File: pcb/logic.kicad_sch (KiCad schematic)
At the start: 8 parts, among them U3 74HC02, U4 74HC08, U5 74HC02

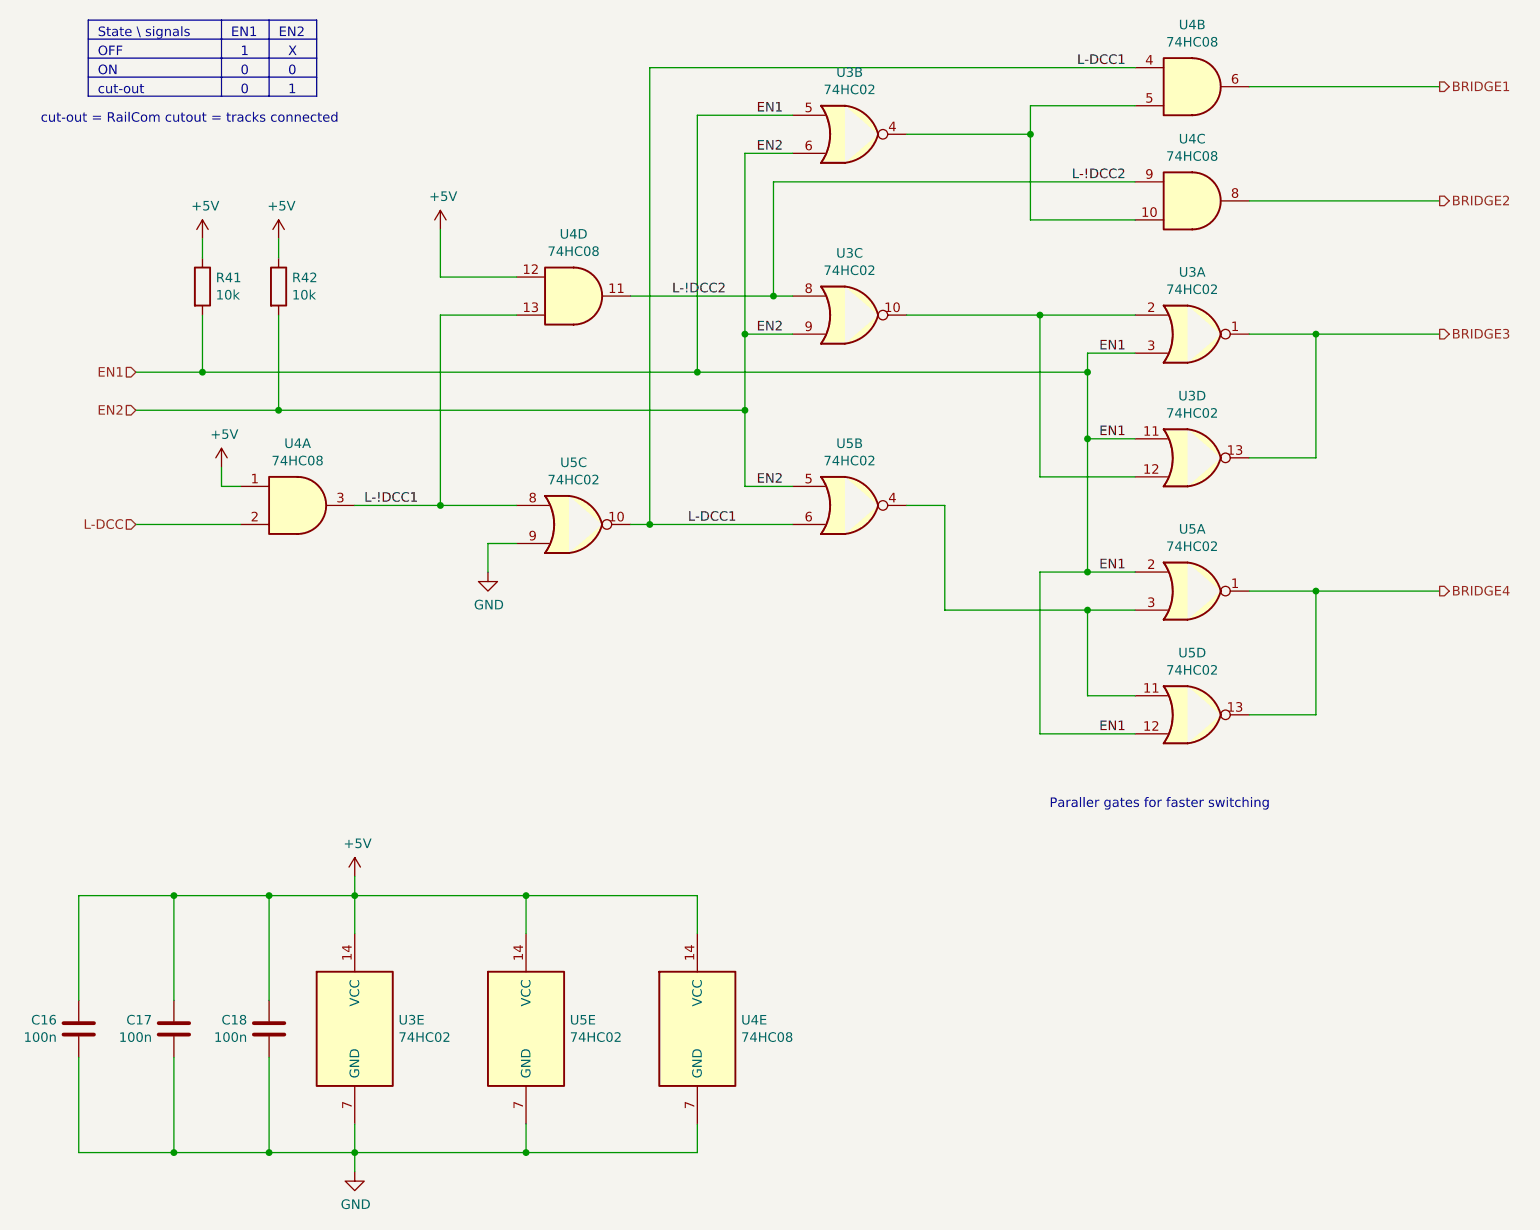
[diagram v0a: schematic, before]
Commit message: Update to KiCad 8.
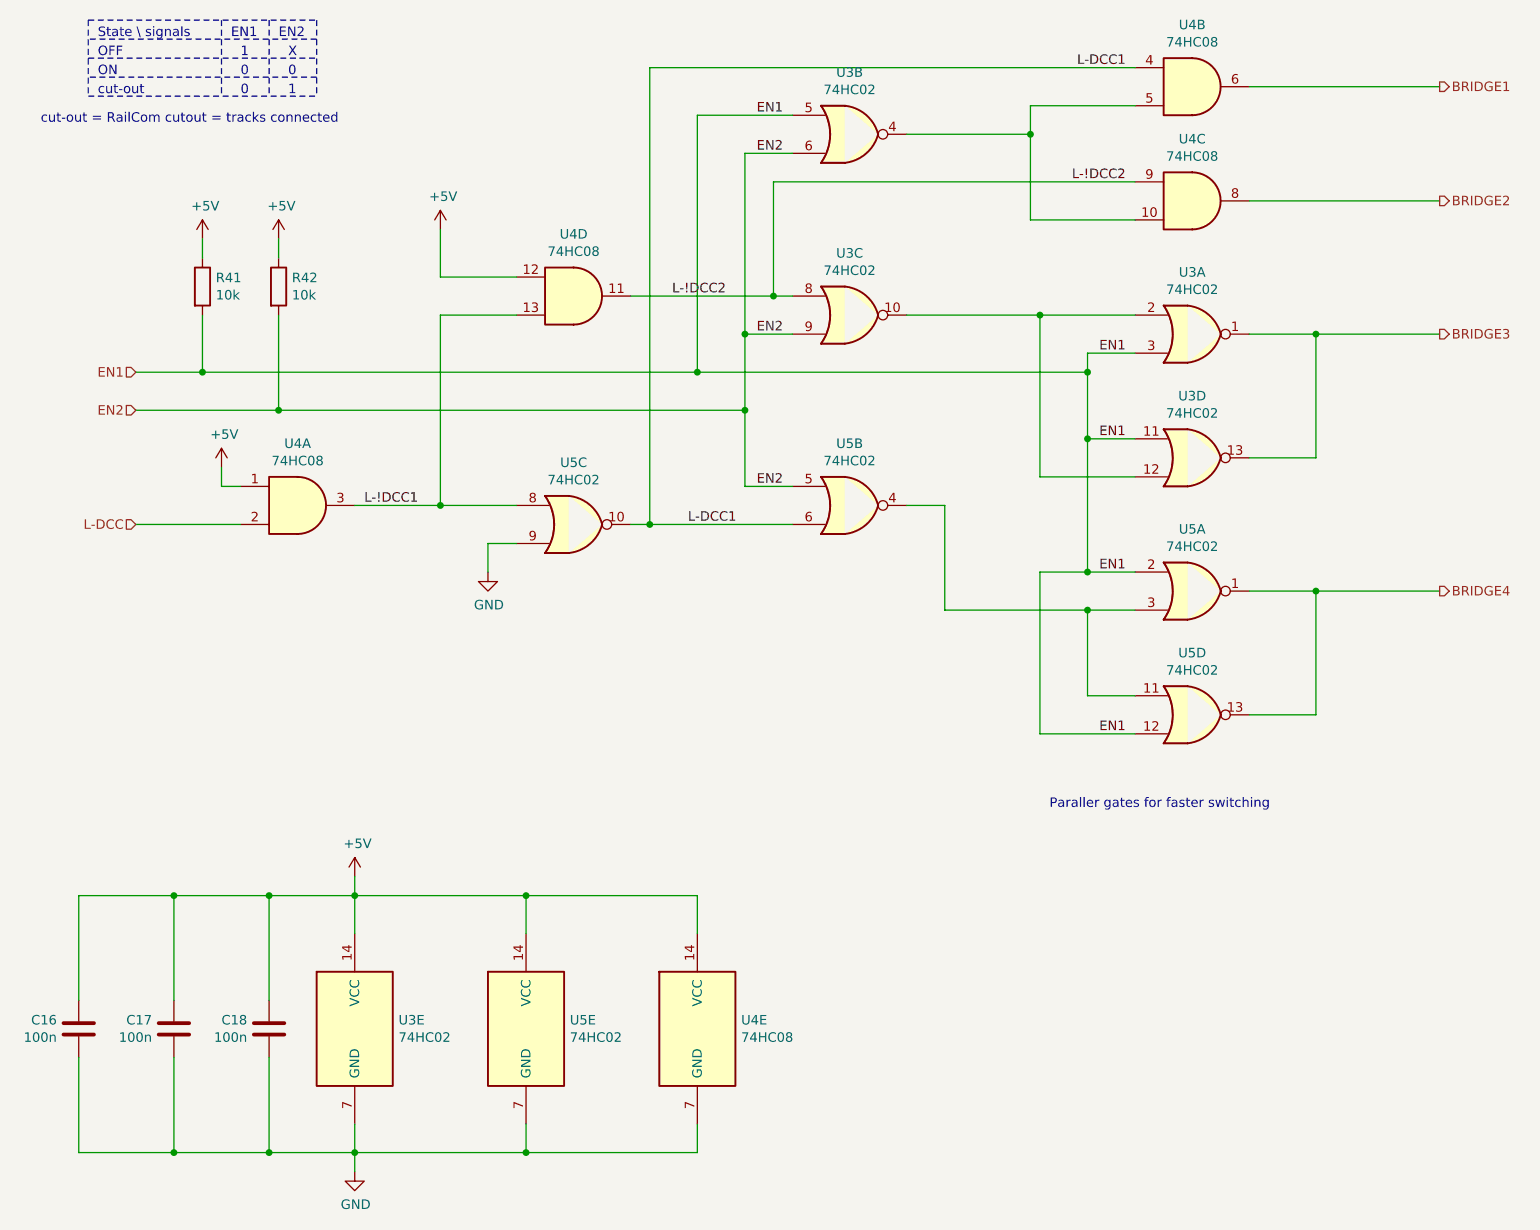
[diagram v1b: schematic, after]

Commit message: Export root page escription to other pages.
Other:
- company: (none) -> Model Railroader Club Brno I – KMŽ Brno I – https://kmz-brno.cz/
- title: HB22 – logic -> HB22 – DCC booster
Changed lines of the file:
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@@
 	(paper "A4")
 	(title_block
-		(title "HB22 – logic")
-		(comment 4 "Create control signal for H-bridge based on DCC and current state.")
+		(title "HB22 – DCC booster")
+		(date "2025-02-20")
+		(rev "1.0")
+		(company "Model Railroader Club Brno I – KMŽ Brno I – https://kmz-brno.cz/")
+		(comment 1 "Jan Horáček")
+		(comment 2 "https://github.com/kmzbrnoI/hb22")
+		(comment 3 "https://creativecommons.org/licenses/by-sa/4.0/")
+		(comment 4 "Released under the Creative Commons Attribution-ShareAlike 4.0 License")
 	)
 	(junction

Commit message: Use normal SMD footprints, avoid handsolder.
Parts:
- C16, C17, C18: footprint Capacitor_SMD:C_0805_2012Metric_Pad1.18x1.45mm_HandSolder -> Capacitor_SMD:C_0805_2012Metric
- R41, R42: footprint Resistor_SMD:R_0805_2012Metric_Pad1.20x1.40mm_HandSolder -> Resistor_SMD:R_0805_2012Metric
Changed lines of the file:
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@@
 			)
 		)
-		(property "Footprint" "Capacitor_SMD:C_0805_2012Metric_Pad1.18x1.45mm_HandSolder"
+		(property "Footprint" "Capacitor_SMD:C_0805_2012Metric"
 			(at 74.6252 160.02 0)
 			(effects
@@
 			)
 		)
-		(property "Footprint" "Capacitor_SMD:C_0805_2012Metric_Pad1.18x1.45mm_HandSolder"
+		(property "Footprint" "Capacitor_SMD:C_0805_2012Metric"
 			(at 61.9252 160.02 0)
 			(effects
@@
 			)
 		)
-		(property "Footprint" "Capacitor_SMD:C_0805_2012Metric_Pad1.18x1.45mm_HandSolder"
+		(property "Footprint" "Capacitor_SMD:C_0805_2012Metric"
 			(at 49.2252 160.02 0)
 			(effects
@@
 			)
 		)
-		(property "Footprint" "Resistor_SMD:R_0805_2012Metric_Pad1.20x1.40mm_HandSolder"
+		(property "Footprint" "Resistor_SMD:R_0805_2012Metric"
 			(at 62.992 64.77 90)
 			(effects
@@
 			)
 		)
-		(property "Footprint" "Resistor_SMD:R_0805_2012Metric_Pad1.20x1.40mm_HandSolder"
+		(property "Footprint" "Resistor_SMD:R_0805_2012Metric"
 			(at 73.152 64.77 90)
 			(effects
